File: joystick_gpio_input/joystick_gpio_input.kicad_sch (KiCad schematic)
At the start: 22 parts, among them J1 Conn_01x06, J2 Conn_01x04, J3 Conn_01x15, J4 Conn_01x15_Male, J5 Conn_01x15_Male

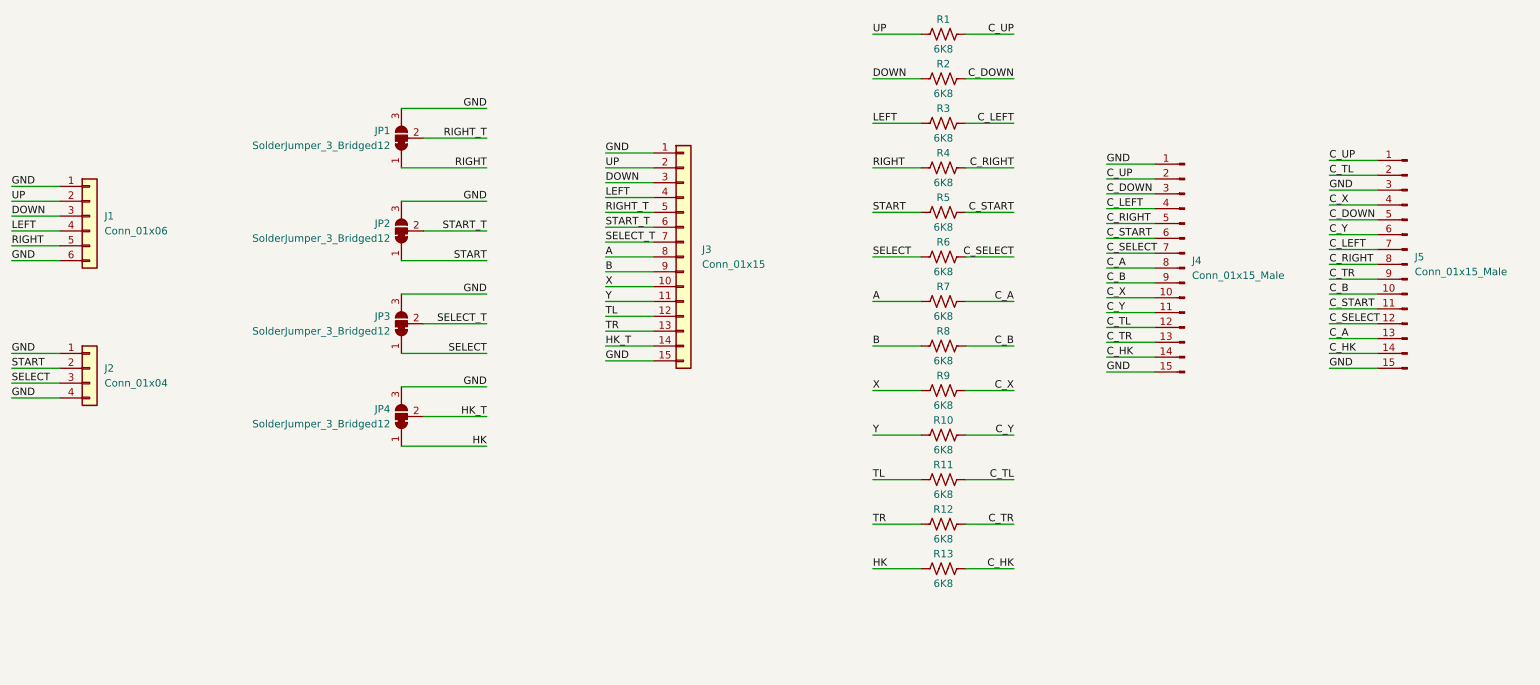
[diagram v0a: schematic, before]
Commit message: gpio 입력 보드 점퍼 변경
Signed-off-by: Ju, Gyeong-min <jcmh74@gmail.com>
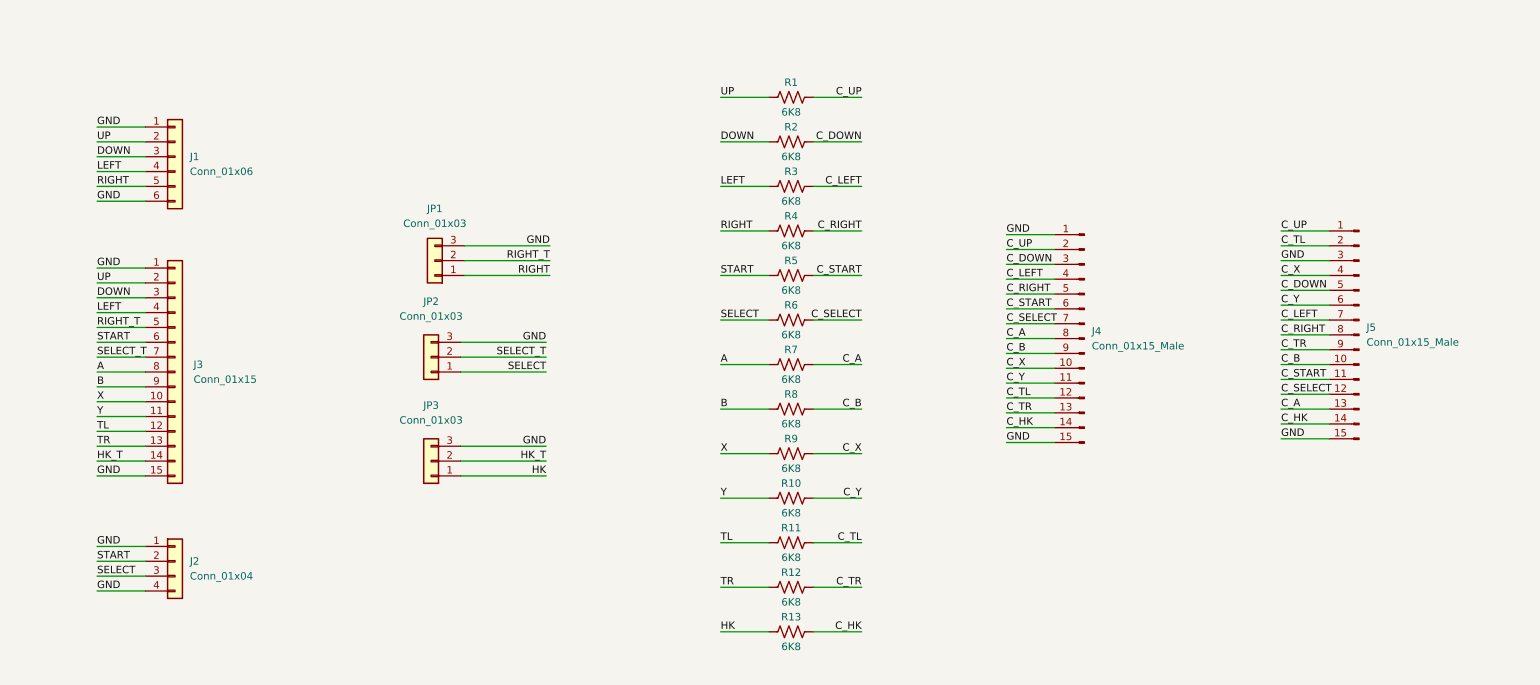
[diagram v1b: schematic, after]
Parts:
- removed JP2: SolderJumper_3_Bridged12, Jumper:SolderJumper-3_P1.3mm_Bridged12_Pad1.0x1.5mm, symbol Jumper:SolderJumper_3_Bridged12
- JP1: value SolderJumper_3_Bridged12 -> Conn_01x03; footprint Jumper:SolderJumper-3_P1.3mm_Bridged12_Pad1.0x1.5mm -> Connector_PinHeader_2.54mm:PinHeader_1x03_P2.54mm_Vertical; symbol Jumper:SolderJumper_3_Bridged12 -> Connector_Generic:Conn_01x03
- JP2: renamed from JP3; value SolderJumper_3_Bridged12 -> Conn_01x03; footprint Jumper:SolderJumper-3_P1.3mm_Bridged12_Pad1.0x1.5mm -> Connector_PinHeader_2.54mm:PinHeader_1x03_P2.54mm_Vertical; symbol Jumper:SolderJumper_3_Bridged12 -> Connector_Generic:Conn_01x03
- JP3: renamed from JP4; value SolderJumper_3_Bridged12 -> Conn_01x03; footprint Jumper:SolderJumper-3_P1.3mm_Bridged12_Pad1.0x1.5mm -> Connector_PinHeader_2.54mm:PinHeader_1x03_P2.54mm_Vertical; symbol Jumper:SolderJumper_3_Bridged12 -> Connector_Generic:Conn_01x03
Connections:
- net START_T is gone; now on net START: J3.6 (Pin_6)
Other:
- moved on the sheet: J1, J2, J3, J4, J5, R1, R10, R11, R12, R13, R2, R3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

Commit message: gpio input 보드 크기 조정
Signed-off-by: Ju, Gyeong-min <jcmh74@gmail.com>
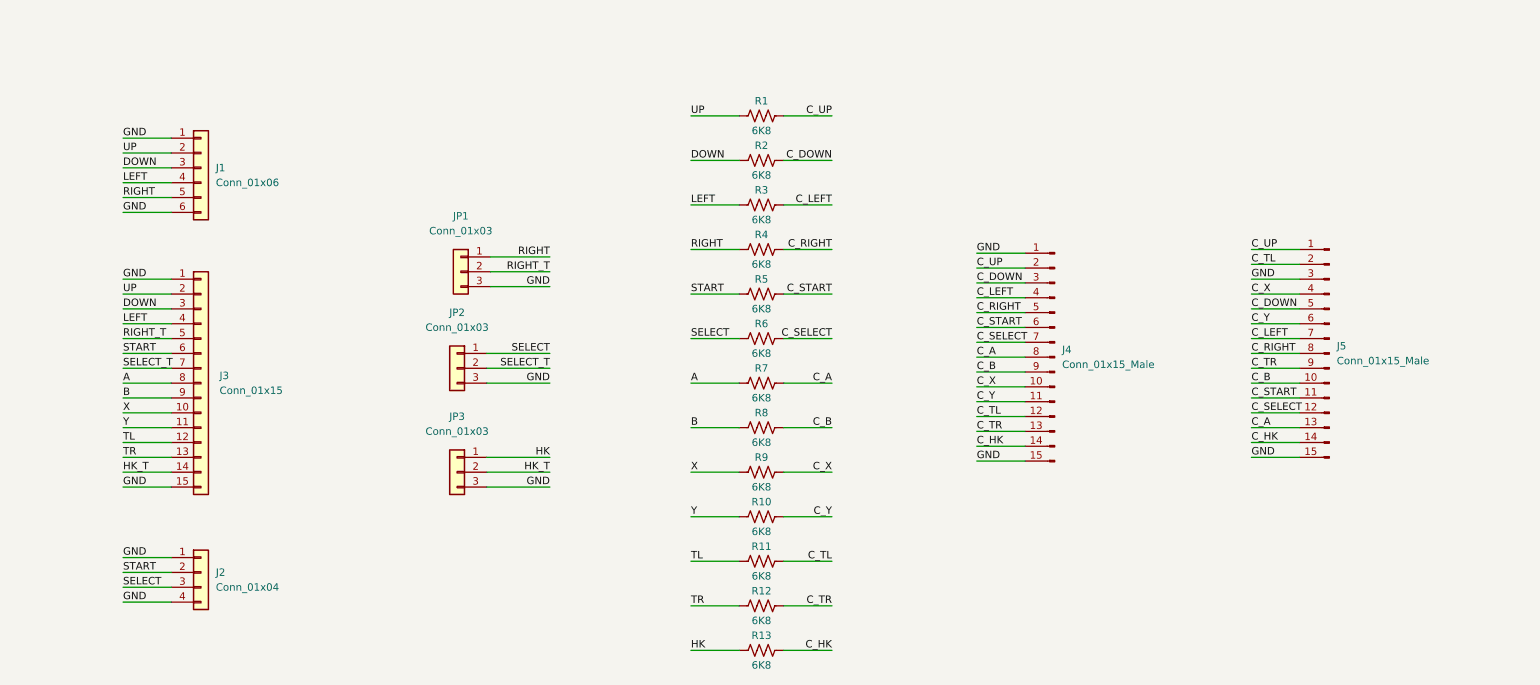
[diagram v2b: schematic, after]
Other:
- moved on the sheet: J1, J2, J3, J4, J5, JP1, JP2, JP3, R1, R10, R11, R12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

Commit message: gpio 입력 보드 확장
Signed-off-by: Ju, Gyeong-min <jcmh74@gmail.com>
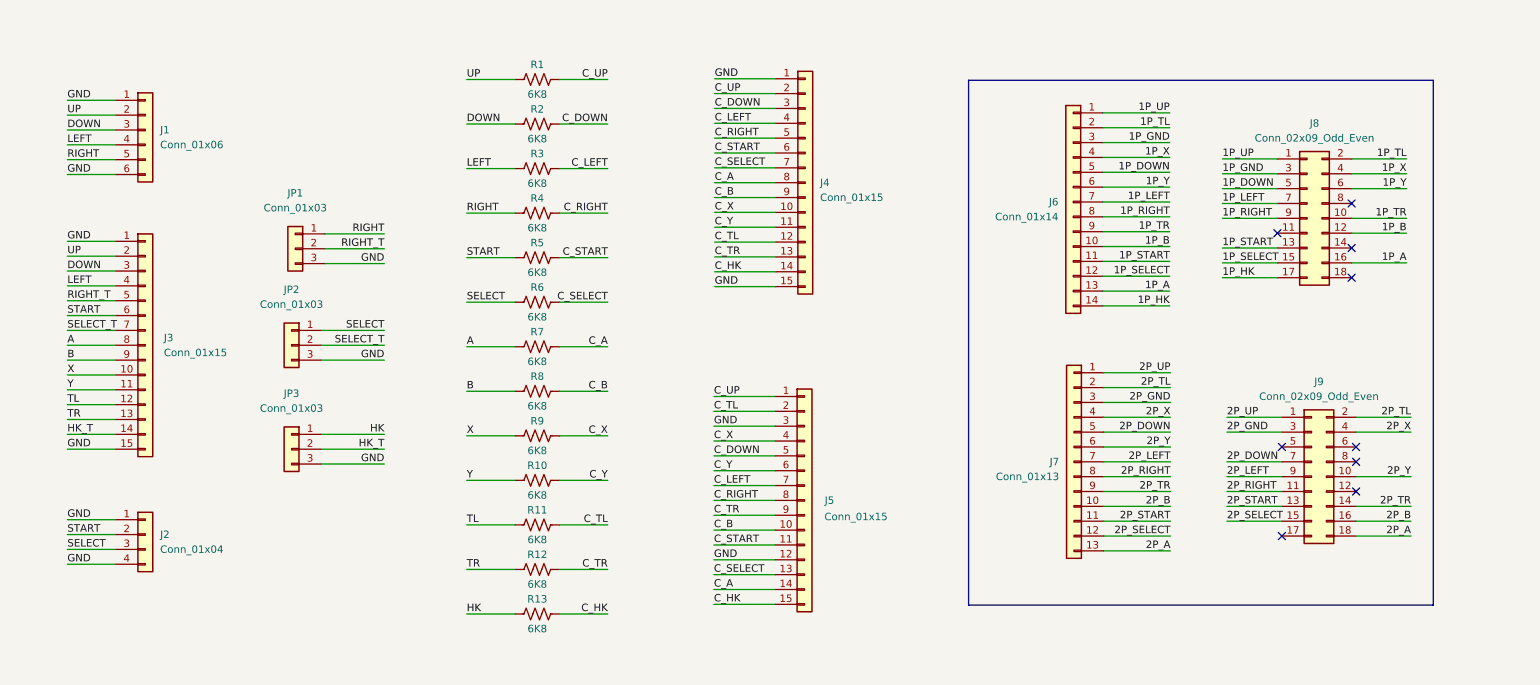
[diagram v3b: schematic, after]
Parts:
- added J6: Conn_01x14, Connector_Molex:Molex_PicoBlade_53047-1410_1x14_P1.25mm_Vertical, symbol Connector_Generic:Conn_01x14
- added J7: Conn_01x13, Connector_Molex:Molex_PicoBlade_53047-1310_1x13_P1.25mm_Vertical, symbol Connector_Generic:Conn_01x13
- added J8, J9: Conn_02x09_Odd_Even, Connector_PinSocket_2.54mm:PinSocket_2x09_P2.54mm_Vertical, symbol Connector_Generic:Conn_02x09_Odd_Even
- J4, J5: value Conn_01x15_Male -> Conn_01x15; symbol Connector:Conn_01x15_Male -> Connector_Generic:Conn_01x15
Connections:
- net C_A: now also J5.14 (Pin_14); no longer J5.13 (Pin_13)
- net C_HK: now also J5.15 (Pin_15); no longer J5.14 (Pin_14)
- net C_SELECT: now also J5.13 (Pin_13); no longer J5.12 (Pin_12)
- net GND: now also J5.12 (Pin_12); no longer J5.15 (Pin_15)
- new net 1P_A: J6.13 (Pin_13), J8.16 (Pin_16)
- new net 1P_B: J6.10 (Pin_10), J8.12 (Pin_12)
- new net 1P_DOWN: J6.5 (Pin_5), J8.5 (Pin_5)
- new net 1P_GND: J6.3 (Pin_3), J8.3 (Pin_3)
- new net 1P_HK: J6.14 (Pin_14), J8.17 (Pin_17)
- new net 1P_LEFT: J6.7 (Pin_7), J8.7 (Pin_7)
- new net 1P_RIGHT: J6.8 (Pin_8), J8.9 (Pin_9)
- new net 1P_SELECT: J6.12 (Pin_12), J8.15 (Pin_15)
- new net 1P_START: J6.11 (Pin_11), J8.13 (Pin_13)
- new net 1P_TL: J6.2 (Pin_2), J8.2 (Pin_2)
- new net 1P_TR: J6.9 (Pin_9), J8.10 (Pin_10)
- new net 1P_UP: J6.1 (Pin_1), J8.1 (Pin_1)
- new net 1P_X: J6.4 (Pin_4), J8.4 (Pin_4)
- new net 1P_Y: J6.6 (Pin_6), J8.6 (Pin_6)
- new net 2P_A: J7.13 (Pin_13), J9.18 (Pin_18)
- new net 2P_B: J7.10 (Pin_10), J9.16 (Pin_16)
- new net 2P_DOWN: J7.5 (Pin_5), J9.7 (Pin_7)
- new net 2P_GND: J7.3 (Pin_3), J9.3 (Pin_3)
- new net 2P_LEFT: J7.7 (Pin_7), J9.9 (Pin_9)
- new net 2P_RIGHT: J7.8 (Pin_8), J9.11 (Pin_11)
- new net 2P_SELECT: J7.12 (Pin_12), J9.15 (Pin_15)
- new net 2P_START: J7.11 (Pin_11), J9.13 (Pin_13)
- new net 2P_TL: J7.2 (Pin_2), J9.2 (Pin_2)
- new net 2P_TR: J7.9 (Pin_9), J9.14 (Pin_14)
- new net 2P_UP: J7.1 (Pin_1), J9.1 (Pin_1)
- new net 2P_X: J7.4 (Pin_4), J9.4 (Pin_4)
- new net 2P_Y: J7.6 (Pin_6), J9.10 (Pin_10)
- no-connect marks 0 -> 9
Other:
- moved on the sheet: J1, J2, J3, JP1, JP2, JP3, R1, R10, R11, R12, R13, R2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

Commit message: gpio 입력 보드 커넥터 1개씩 늘림
Signed-off-by: Ju, Gyeong-min <jcmh74@gmail.com>
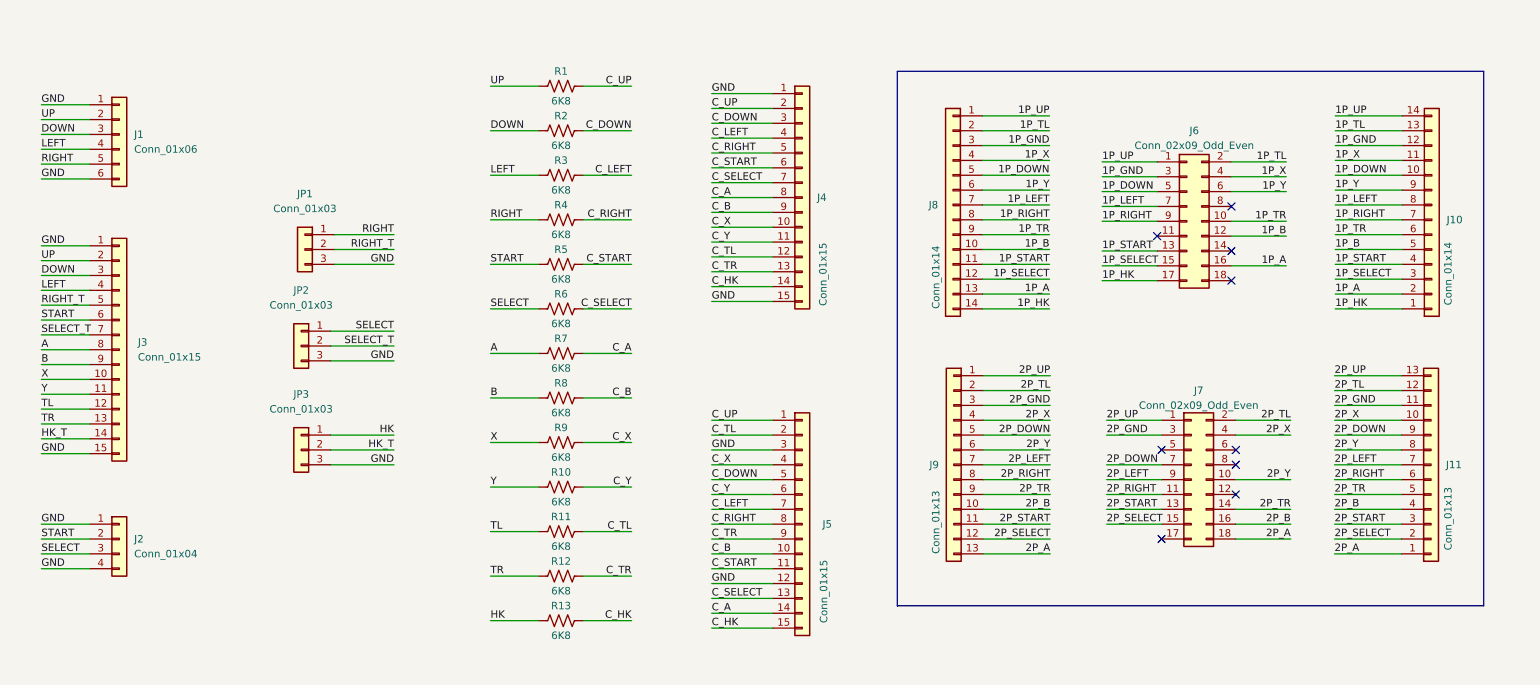
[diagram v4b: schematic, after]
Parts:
- added J10: Conn_01x14, joystick_gpio_input_library:conn_ex_1x14_P1.25mm_Vertical, symbol Connector_Generic:Conn_01x14
- added J11: Conn_01x13, joystick_gpio_input_library:conn_ex_1x13_P1.25mm_Vertical, symbol Connector_Generic:Conn_01x13
- J8: renamed from J6; footprint Connector_Molex:Molex_PicoBlade_53047-1410_1x14_P1.25mm_Vertical -> joystick_gpio_input_library:conn_ex_1x14_P1.25mm_Vertical
- J9: renamed from J7; footprint Connector_Molex:Molex_PicoBlade_53047-1310_1x13_P1.25mm_Vertical -> joystick_gpio_input_library:conn_ex_1x13_P1.25mm_Vertical
- renumbered J8 to J6, J9 to J7
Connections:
- net 1P_A: now also J10.2 (Pin_2)
- net 1P_B: now also J10.5 (Pin_5)
- net 1P_DOWN: now also J10.10 (Pin_10)
- net 1P_GND: now also J10.12 (Pin_12)
- net 1P_HK: now also J10.1 (Pin_1)
- net 1P_LEFT: now also J10.8 (Pin_8)
- net 1P_RIGHT: now also J10.7 (Pin_7)
- net 1P_SELECT: now also J10.3 (Pin_3)
- net 1P_START: now also J10.4 (Pin_4)
- net 1P_TL: now also J10.13 (Pin_13)
- net 1P_TR: now also J10.6 (Pin_6)
- net 1P_UP: now also J10.14 (Pin_14)
- net 1P_X: now also J10.11 (Pin_11)
- net 1P_Y: now also J10.9 (Pin_9)
- net 2P_A: now also J11.1 (Pin_1)
- net 2P_B: now also J11.4 (Pin_4)
- net 2P_DOWN: now also J11.9 (Pin_9)
- net 2P_GND: now also J11.11 (Pin_11)
- net 2P_LEFT: now also J11.7 (Pin_7)
- net 2P_RIGHT: now also J11.6 (Pin_6)
- net 2P_SELECT: now also J11.2 (Pin_2)
- net 2P_START: now also J11.3 (Pin_3)
- net 2P_TL: now also J11.12 (Pin_12)
- net 2P_TR: now also J11.5 (Pin_5)
- net 2P_UP: now also J11.13 (Pin_13)
- net 2P_X: now also J11.10 (Pin_10)
- net 2P_Y: now also J11.8 (Pin_8)
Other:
- moved on the sheet: J1, J2, J3, J4, J5, J6, J7, J8, J9, JP1, JP2, JP3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

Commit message: Rev 2 설계
Signed-off-by: Ju, Gyeong-min <jcmh74@gmail.com>
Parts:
- added J12: Conn_01x15, Connector_PinHeader_2.54mm:PinHeader_1x15_P2.54mm_Vertical, symbol Connector_Generic:Conn_01x15
- J10: footprint joystick_gpio_input_library:conn_ex_1x14_P1.25mm_Vertical -> joystick_gpio_input_library:conn_ex_1x14_P1.25mm_Vertical_Left_Labeled
- J11: footprint joystick_gpio_input_library:conn_ex_1x13_P1.25mm_Vertical -> joystick_gpio_input_library:conn_ex_1x13_P1.25mm_Vertical_Left_Labeled
- J5: value Conn_01x15 -> Conn_01x14; footprint Connector_PinHeader_2.54mm:PinHeader_1x15_P2.54mm_Vertical -> joystick_gpio_input_library:conn_ex_1x14_P1.25mm_Vertical_Left_Labeled; symbol Connector_Generic:Conn_01x15 -> Connector_Generic:Conn_01x14
- J8: footprint joystick_gpio_input_library:conn_ex_1x14_P1.25mm_Vertical -> joystick_gpio_input_library:conn_ex_1x14_P1.25mm_Vertical_Right_Labeled
- J9: footprint joystick_gpio_input_library:conn_ex_1x13_P1.25mm_Vertical -> joystick_gpio_input_library:conn_ex_1x13_P1.25mm_Vertical_Right_Labeled
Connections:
- net 1P_A: now also J10.12 (Pin_12), J8.12 (Pin_12); no longer J10.2 (Pin_2), J8.13 (Pin_13)
- net 1P_B: now also J10.9 (Pin_9), J8.9 (Pin_9); no longer J10.5 (Pin_5), J8.10 (Pin_10)
- net 1P_DOWN: now also J10.4 (Pin_4), J8.4 (Pin_4); no longer J10.10 (Pin_10), J8.5 (Pin_5)
- net 1P_GND: now also J10.13 (Pin_13), J6.14 (Pin_14), J6.8 (Pin_8), J8.13 (Pin_13); no longer J10.12 (Pin_12), J8.3 (Pin_3)
- net 1P_HK: now also J10.14 (Pin_14); no longer J10.1 (Pin_1)
- net 1P_LEFT: now also J10.6 (Pin_6), J8.6 (Pin_6); no longer J10.8 (Pin_8), J8.7 (Pin_7)
- net 1P_RIGHT: now also J8.7 (Pin_7); no longer J8.8 (Pin_8)
- net 1P_SELECT: now also J10.11 (Pin_11), J8.11 (Pin_11); no longer J10.3 (Pin_3), J8.12 (Pin_12)
- net 1P_START: now also J10.10 (Pin_10), J8.10 (Pin_10); no longer J10.4 (Pin_4), J8.11 (Pin_11)
- net 1P_TL: now also J10.2 (Pin_2); no longer J10.13 (Pin_13)
- net 1P_TR: now also J10.8 (Pin_8), J8.8 (Pin_8); no longer J10.6 (Pin_6), J8.9 (Pin_9)
- net 1P_UP: now also J10.1 (Pin_1); no longer J10.14 (Pin_14)
- net 1P_X: now also J10.3 (Pin_3), J8.3 (Pin_3); no longer J10.11 (Pin_11), J8.4 (Pin_4)
- net 1P_Y: now also J10.5 (Pin_5), J8.5 (Pin_5); no longer J10.9 (Pin_9), J8.6 (Pin_6)
- net 2P_A: now also J11.12 (Pin_12), J9.12 (Pin_12); no longer J11.1 (Pin_1), J9.13 (Pin_13)
- net 2P_B: now also J11.9 (Pin_9), J9.9 (Pin_9); no longer J11.4 (Pin_4), J9.10 (Pin_10)
- net 2P_DOWN: now also J11.4 (Pin_4), J9.4 (Pin_4); no longer J11.9 (Pin_9), J9.5 (Pin_5)
- net 2P_GND: now also J11.13 (Pin_13), J7.12 (Pin_12), J7.17 (Pin_17), J7.8 (Pin_8), J9.13 (Pin_13); no longer J11.11 (Pin_11), J9.3 (Pin_3)
- net 2P_LEFT: now also J11.6 (Pin_6), J9.6 (Pin_6); no longer J11.7 (Pin_7), J9.7 (Pin_7)
- net 2P_RIGHT: now also J11.7 (Pin_7), J9.7 (Pin_7); no longer J11.6 (Pin_6), J9.8 (Pin_8)
- net 2P_SELECT: now also J11.11 (Pin_11), J9.11 (Pin_11); no longer J11.2 (Pin_2), J9.12 (Pin_12)
- net 2P_START: now also J11.10 (Pin_10), J9.10 (Pin_10); no longer J11.3 (Pin_3), J9.11 (Pin_11)
- net 2P_TL: now also J11.2 (Pin_2); no longer J11.12 (Pin_12)
- net 2P_TR: now also J11.8 (Pin_8), J9.8 (Pin_8); no longer J11.5 (Pin_5), J9.9 (Pin_9)
- net 2P_UP: now also J11.1 (Pin_1); no longer J11.13 (Pin_13)
- net 2P_X: now also J11.3 (Pin_3), J9.3 (Pin_3); no longer J11.10 (Pin_10), J9.4 (Pin_4)
- net 2P_Y: now also J11.5 (Pin_5), J9.5 (Pin_5); no longer J11.8 (Pin_8), J9.6 (Pin_6)
- net A: now also J12.8 (Pin_8)
- net B: now also J12.9 (Pin_9)
- net C_A: now also J5.12 (Pin_12); no longer J5.14 (Pin_14)
- net C_B: now also J5.9 (Pin_9); no longer J5.10 (Pin_10)
- net C_DOWN: now also J5.4 (Pin_4); no longer J5.5 (Pin_5)
- net C_HK: now also J5.14 (Pin_14); no longer J5.15 (Pin_15)
- net C_LEFT: now also J5.6 (Pin_6); no longer J5.7 (Pin_7)
- net C_RIGHT: now also J5.7 (Pin_7); no longer J5.8 (Pin_8)
- net C_SELECT: now also J5.11 (Pin_11); no longer J5.13 (Pin_13)
- net C_START: now also J5.10 (Pin_10); no longer J5.11 (Pin_11)
- net C_TR: now also J5.8 (Pin_8); no longer J5.9 (Pin_9)
- net C_X: now also J5.3 (Pin_3); no longer J5.4 (Pin_4)
- net C_Y: now also J5.5 (Pin_5); no longer J5.6 (Pin_6)
- net DOWN: now also J12.3 (Pin_3)
- net GND: now also J5.13 (Pin_13), J12.1 (Pin_1), J12.15 (Pin_15); no longer J5.12 (Pin_12), J5.3 (Pin_3)
- net HK: now also J12.14 (Pin_14)
- net LEFT: now also J12.4 (Pin_4)
- net RIGHT: now also J12.5 (Pin_5)
- net SELECT: now also J12.7 (Pin_7)
- net START: now also J12.6 (Pin_6)
- net TL: now also J12.12 (Pin_12)
- net TR: now also J12.13 (Pin_13)
- net UP: now also J12.2 (Pin_2)
- net X: now also J12.10 (Pin_10)
- net Y: now also J12.11 (Pin_11)
- no-connect marks 9 -> 4
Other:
- moved on the sheet: JP1, JP2, JP3, R1, R10, R11, R12, R13, R2, R3, R4, R5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
